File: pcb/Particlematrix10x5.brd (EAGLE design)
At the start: 100 x 80 mm, 65 parts

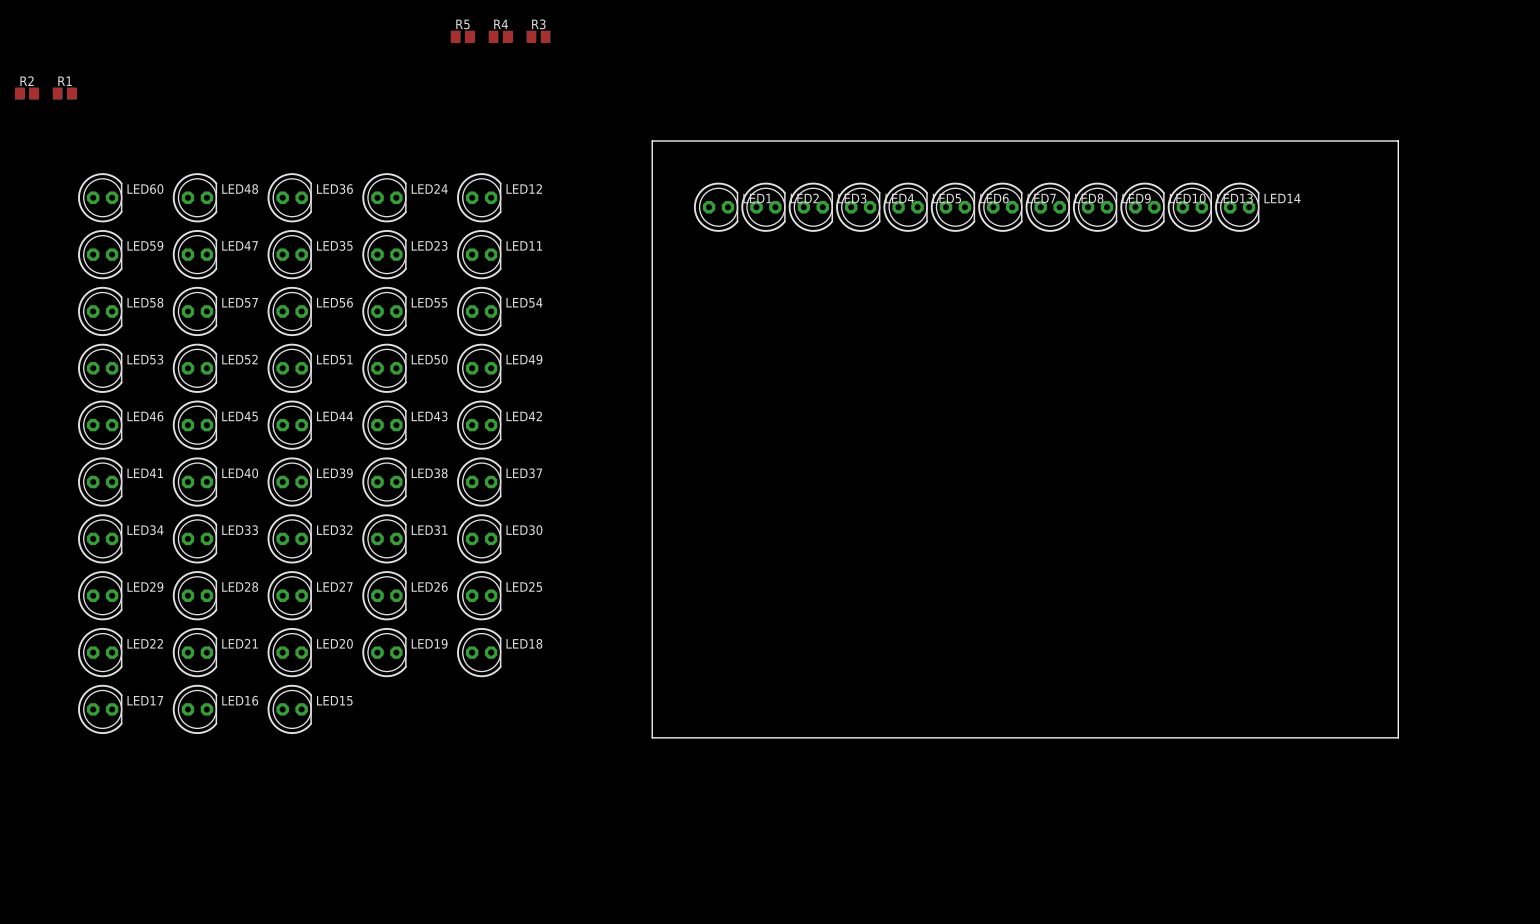
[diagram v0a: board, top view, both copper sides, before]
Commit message: Added 4017 decade counter to schematic
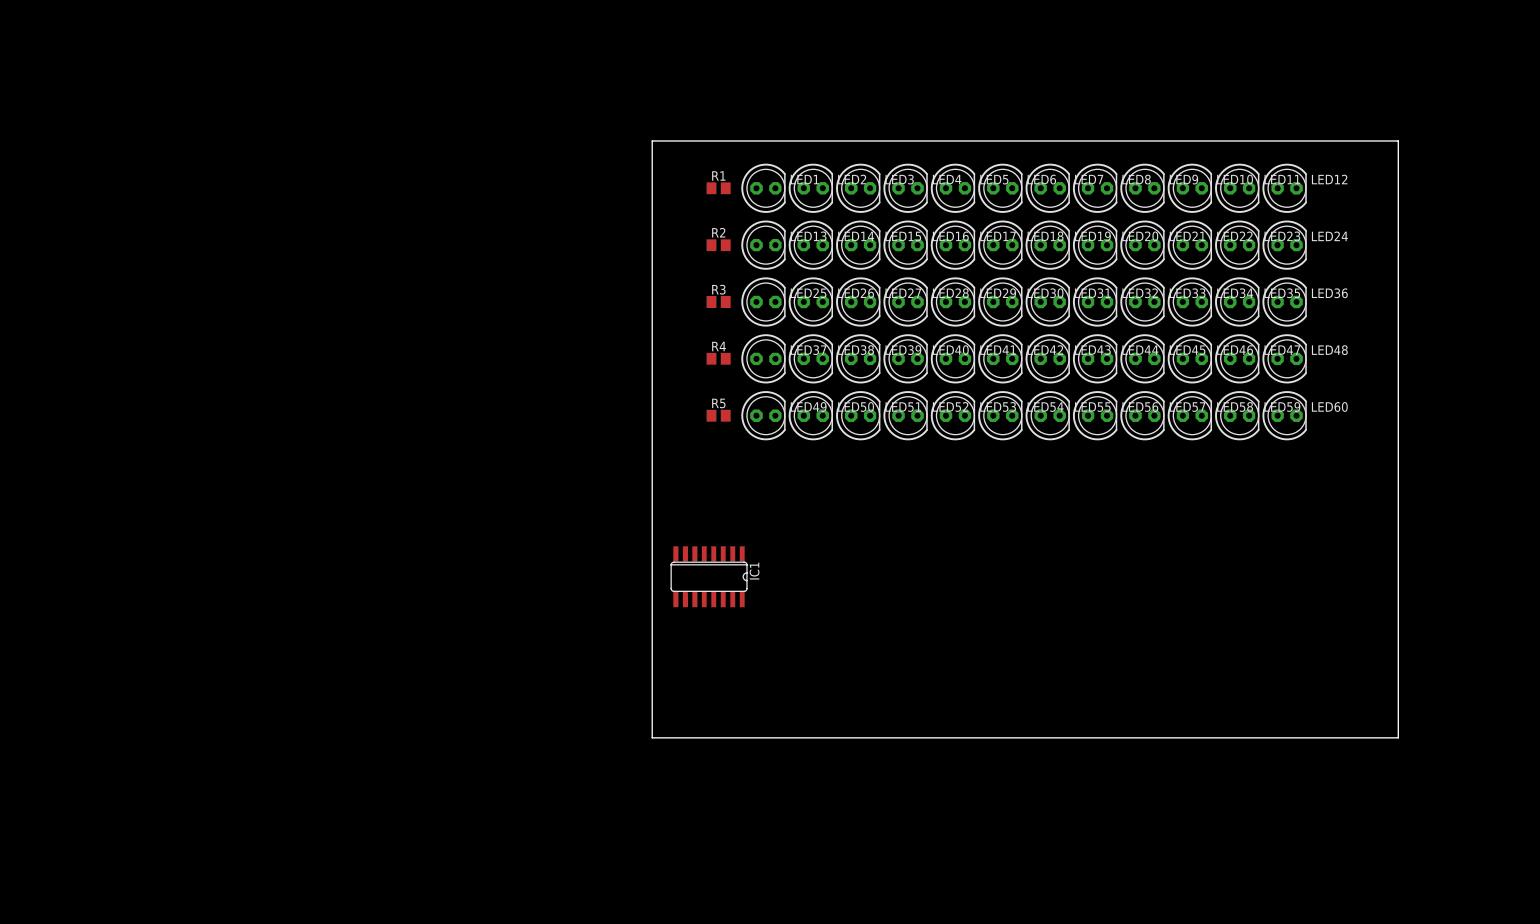
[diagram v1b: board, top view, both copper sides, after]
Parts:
- added IC1: 4017D, 40xx:SO16
- moved LED60 161.4 mm to (85.1, 43.2)
- moved LED22 155.9 mm to (72.4, 66.0)
- moved LED59 153.9 mm to (78.7, 43.2)
- moved LED34 149.5 mm to (72.4, 58.4)
- moved LED48 147.6 mm to (85.1, 50.8)
- moved LED58 146.7 mm to (72.4, 43.2)
- moved LED46 146.3 mm to (72.4, 50.8)
- moved LED47 140.4 mm to (78.7, 50.8)
- moved LED21 138.2 mm to (66.0, 66.0)
- moved LED36 134.1 mm to (85.1, 58.4)
- moved LED33 130.9 mm to (66.0, 58.4)
- moved LED17 130.1 mm to (40.6, 66.0)
- moved LED57 127.8 mm to (66.0, 43.2)
- moved LED45 127.3 mm to (66.0, 50.8)
- moved LED35 127.2 mm to (78.7, 58.4)
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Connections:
- removed net ROW1: R1.1
- removed net ROW2: R2.1
- removed net ROW3: R3.1
- removed net ROW4: R4.1
- removed net ROW5: R5.1
- new net N$1: IC1.3, R1.1
- new net N$2: IC1.2, R2.1
- new net N$3: IC1.4, R3.1
- new net N$4: IC1.7, R4.1
- new net N$5: IC1.10, R5.1
- new net N$6: IC1.1, IC1.15
- new net VDD: IC1.16
- new net VSS: IC1.8

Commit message: Routed all LEDs, decade counter, and Arduino Mega
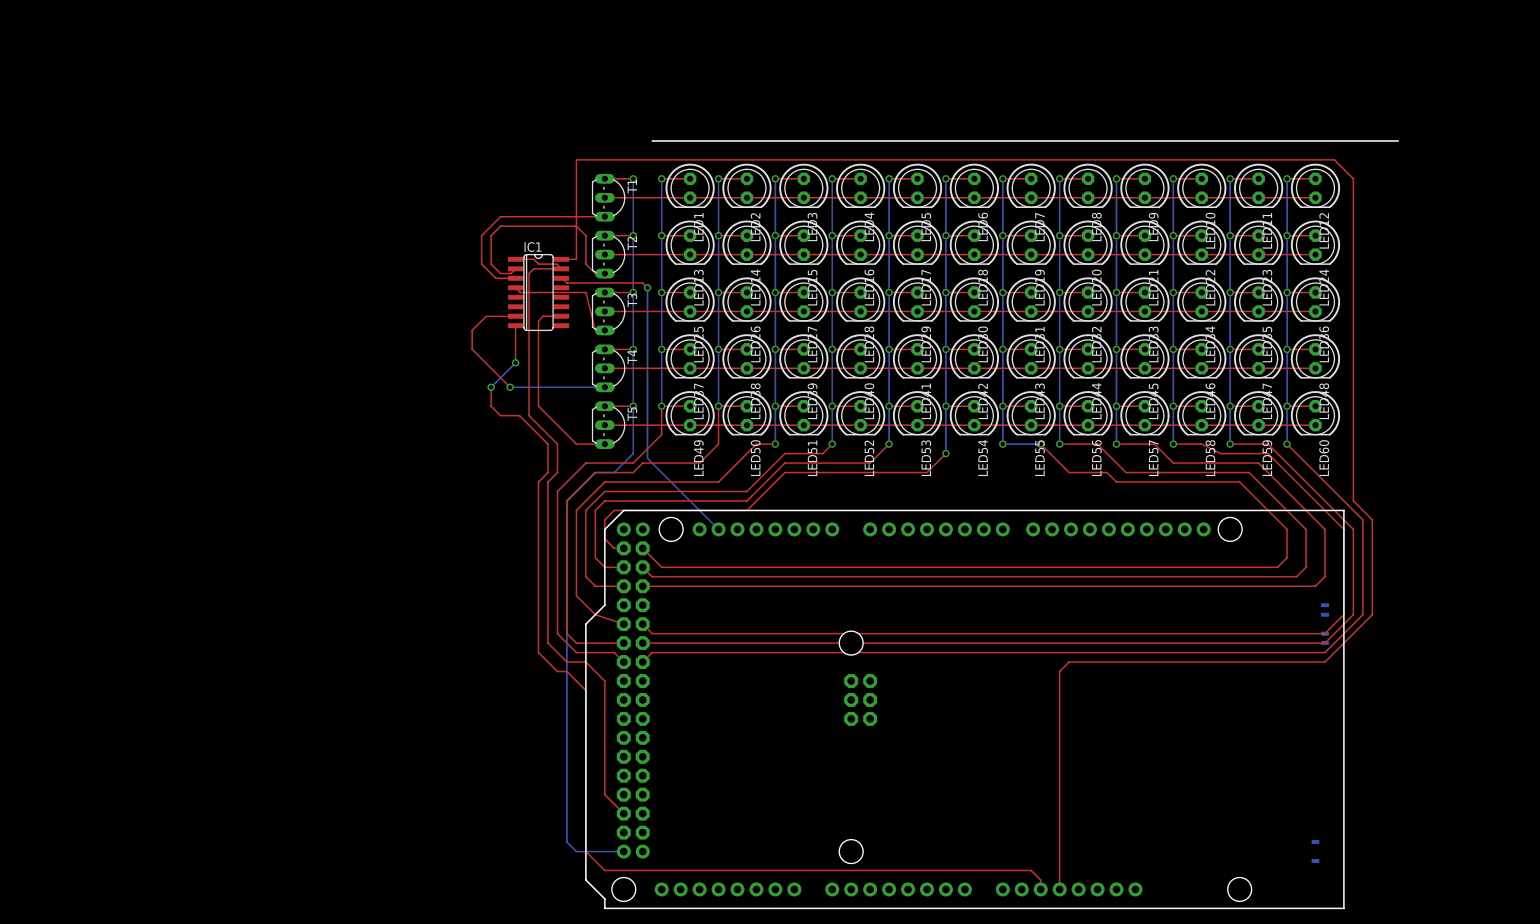
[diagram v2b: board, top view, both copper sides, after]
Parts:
- removed R1, R2, R3, R4, R5: 120, resistor:M0805
- added PCB1: ARDUINO_MEGA2560, E14_Arduino_revB:ARDUINO_MEGA2560
- added T1, T2, T3, T4, T5: (no value), transistor-neu-to92:TO92-EBC
- moved IC1 44.4 mm to (-15.2, 59.7), turned to 270 degrees
- moved LED1 10.2 mm to (5.08, 73.7), turned to 270 degrees
- moved LED13 10.2 mm to (5.08, 66.0), turned to 270 degrees
- moved LED25 10.2 mm to (5.08, 58.4), turned to 270 degrees
- moved LED37 10.2 mm to (5.08, 50.8), turned to 270 degrees
- moved LED49 10.2 mm to (5.08, 43.2), turned to 270 degrees
- moved LED14 8.89 mm to (12.7, 66.0), turned to 270 degrees
- moved LED2 8.89 mm to (12.7, 73.7), turned to 270 degrees
- moved LED26 8.89 mm to (12.7, 58.4), turned to 270 degrees
- moved LED38 8.89 mm to (12.7, 50.8), turned to 270 degrees
- moved LED50 8.89 mm to (12.7, 43.2), turned to 270 degrees
- moved LED15 7.62 mm to (20.3, 66.0), turned to 270 degrees
- moved LED27 7.62 mm to (20.3, 58.4), turned to 270 degrees
- moved LED3 7.62 mm to (20.3, 73.7), turned to 270 degrees
- moved LED39 7.62 mm to (20.3, 50.8), turned to 270 degrees
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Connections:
- removed net $1: LED1.K, LED10.K, LED11.K, LED12.K, LED2.K, LED3.K, LED4.K, LED5.K, LED6.K, LED7.K, LED8.K, LED9.K, R1.2
- removed net $2: LED13.K, LED14.K, LED15.K, LED16.K, LED17.K, LED18.K, LED19.K, LED20.K, LED21.K, LED22.K, LED23.K, LED24.K, R2.2
- removed net $3: LED25.K, LED26.K, LED27.K, LED28.K, LED29.K, LED30.K, LED31.K, LED32.K, LED33.K, LED34.K, LED35.K, LED36.K, R3.2
- removed net $4: LED37.K, LED38.K, LED39.K, LED40.K, LED41.K, LED42.K, LED43.K, LED44.K, LED45.K, LED46.K, LED47.K, LED48.K, R4.2
- removed net $9: LED49.K, LED50.K, LED51.K, LED52.K, LED53.K, LED54.K, LED55.K, LED56.K, LED57.K, LED58.K, LED59.K, LED60.K, R5.2
- removed net VDD: IC1.16
- removed net VSS: IC1.8
- new net GND: PCB1.GND..., PCB1.GND...., T1.E, T2.E, T3.E, T4.E, T5.E
- new net N$7: IC1.14, PCB1.20
- new net N$8: IC1.1, IC1.15, PCB1.51
- new net N$9: IC1.8, PCB1.GND..
- new net ROW1: LED1.K, LED10.K, LED11.K, LED12.K, LED2.K, LED3.K, LED4.K, LED5.K, LED6.K, LED7.K, LED8.K, LED9.K, T1.B
- new net ROW2: LED13.K, LED14.K, LED15.K, LED16.K, LED17.K, LED18.K, LED19.K, LED20.K, LED21.K, LED22.K, LED23.K, LED24.K, T2.B
- new net ROW3: LED25.K, LED26.K, LED27.K, LED28.K, LED29.K, LED30.K, LED31.K, LED32.K, LED33.K, LED34.K, LED35.K, LED36.K, T3.B
- new net ROW4: LED37.K, LED38.K, LED39.K, LED40.K, LED41.K, LED42.K, LED43.K, LED44.K, LED45.K, LED46.K, LED47.K, LED48.K, T4.B
- new net ROW5: LED49.K, LED50.K, LED51.K, LED52.K, LED53.K, LED54.K, LED55.K, LED56.K, LED57.K, LED58.K, LED59.K, LED60.K, T5.B
- net COL1: now also PCB1.35
- net COL10: now also PCB1.30
- net COL11: now also PCB1.32
- net COL12: now also PCB1.34
- net COL2: now also PCB1.33
- net COL3: now also PCB1.31
- net COL4: now also PCB1.27
- net COL5: now also PCB1.25
- net COL6: now also PCB1.23
- net COL7: now also PCB1.22
- net COL8: now also PCB1.24
- net COL9: now also PCB1.26
- net N$1: now also T1.C; no longer R1.1
- net N$2: now also T2.C; no longer R2.1
- net N$3: now also T3.C; no longer R3.1
- net N$4: now also T4.C; no longer R4.1
- net N$5: now also T5.C; no longer R5.1
- net N$6: now also IC1.16, PCB1.5V; no longer IC1.1, IC1.15
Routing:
- net N$6: track 0.00 -> 254.3 mm
- net COL7: track 0.00 -> 189.2 mm, vias 0 -> 7
- net COL10: track 0.00 -> 189.0 mm, vias 0 -> 6
- net COL8: track 0.00 -> 187.4 mm, vias 0 -> 6
- net COL9: track 0.00 -> 185.6 mm, vias 0 -> 6
- net COL11: track 0.00 -> 184.1 mm, vias 0 -> 6
- net COL12: track 0.00 -> 180.8 mm, vias 0 -> 6
- net N$9: track 0.00 -> 144.2 mm, vias 0 -> 2
- net GND: track 0.00 -> 121.3 mm, vias 0 -> 5
- net COL6: track 0.00 -> 110.9 mm, vias 0 -> 6
- net COL5: track 0.00 -> 108.3 mm, vias 0 -> 6
- net COL2: track 0.00 -> 107.8 mm, vias 0 -> 5
- net COL4: track 0.00 -> 105.8 mm, vias 0 -> 6
- net COL3: track 0.00 -> 104.0 mm, vias 0 -> 6
- net COL1: track 0.00 -> 100.0 mm, vias 0 -> 5
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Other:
- board size 100 x 80 mm -> 101.6 x 53.3 mm

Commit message: Fix routing errors on pcb
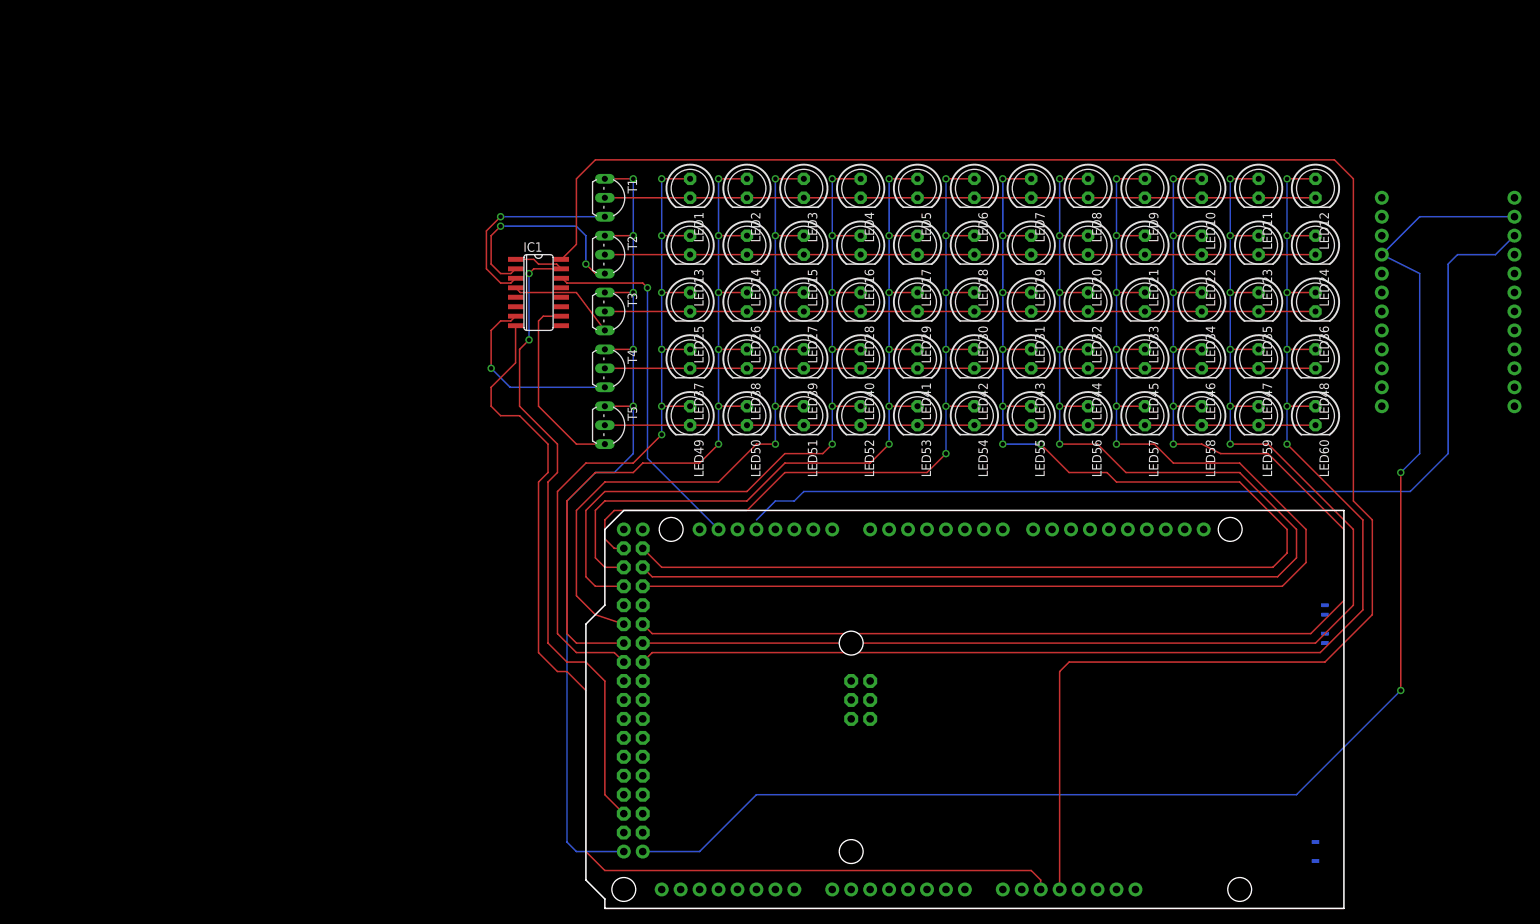
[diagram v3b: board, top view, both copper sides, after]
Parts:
- added U$1: SPARK_CORECORE, Spark:SPARK_CORE
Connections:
- new net N$10: PCB1.18, U$1.3
- new net RAW: U$1.1
- new net VCC: U$1.24
- new net VDDA: U$1.22
- net GND: now also U$1.2, U$1.21
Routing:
- net GND: track 121.3 -> 314.3 mm, vias 5 -> 7
- net N$10: track 0.00 -> 132.3 mm
- net COL9: track 185.6 -> 179.4 mm
- net N$4: track 29.1 -> 25.4 mm
- net COL8: track 187.4 -> 184.1 mm
- net N$6: track 254.3 -> 251.6 mm
- net N$3: track 16.2 -> 14.8 mm
- net COL10: track 189.0 -> 187.9 mm
- net N$8: track 91.5 -> 92.5 mm, vias 0 -> 2
- net COL11: track 184.1 -> 183.4 mm
- net N$1: vias 0 -> 1
- net N$9: vias 2 -> 0
- net N$2: vias 0 -> 2
- net COL2: vias 5 -> 6
- net COL1: vias 5 -> 6

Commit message: Mirrored Arduino and Spark Core again to face front; rerouted
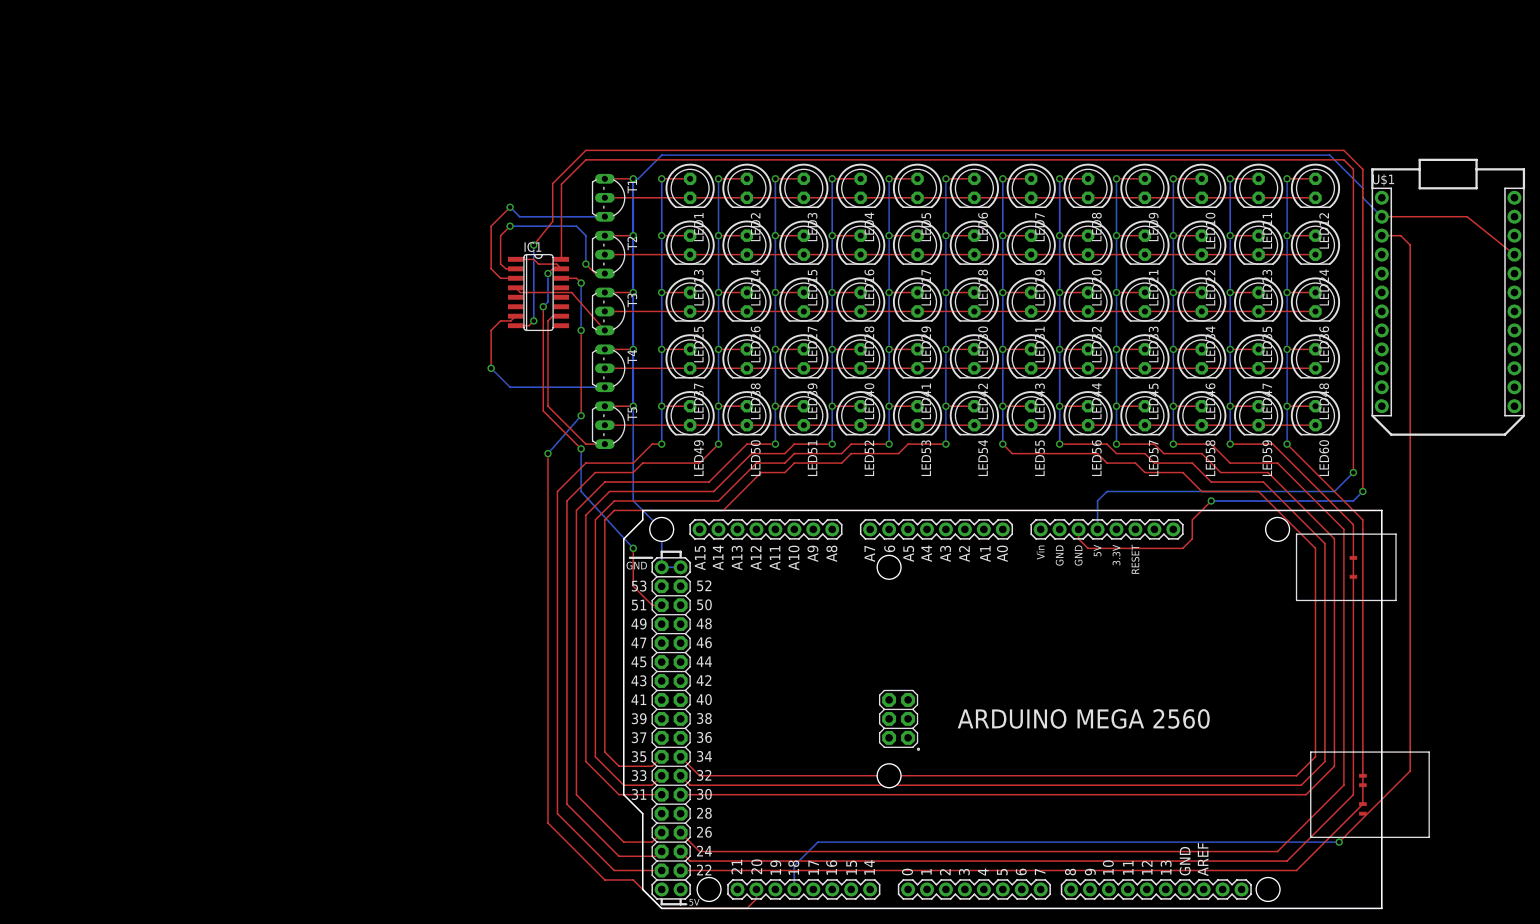
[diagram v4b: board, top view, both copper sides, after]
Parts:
- moved PCB1 53.6 mm to (97.8, 30.5), flipped to the top, turned to 180 degrees
- flipped U$1 to the top
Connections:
- net COL1: now also PCB1.23; no longer PCB1.35
- net COL10: now also PCB1.26; no longer PCB1.30
- net COL11: now also PCB1.24; no longer PCB1.32
- net COL12: now also PCB1.22; no longer PCB1.34
- net COL2: now also PCB1.25; no longer PCB1.33
- net COL3: now also PCB1.27; no longer PCB1.31
- net COL4: now also PCB1.31; no longer PCB1.27
- net COL5: now also PCB1.33; no longer PCB1.25
- net COL6: now also PCB1.35; no longer PCB1.23
- net COL7: now also PCB1.34; no longer PCB1.22
- net COL8: now also PCB1.32; no longer PCB1.24
- net COL9: now also PCB1.30; no longer PCB1.26
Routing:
- net N$9: track 144.2 -> 221.2 mm, vias 0 -> 4
- net N$7: track 48.3 -> 111.4 mm, vias 1 -> 4
- net GND: track 314.3 -> 253.9 mm, vias 7 -> 5
- net N$6: track 251.6 -> 198.4 mm, vias 0 -> 1
- net COL6: track 110.9 -> 144.6 mm
- net COL3: track 104.0 -> 137.6 mm
- net N$10: track 132.3 -> 165.8 mm, vias 0 -> 1
- net COL5: track 108.3 -> 140.9 mm
- net N$8: track 92.5 -> 60.6 mm, vias 2 -> 4
- net COL1: track 100.0 -> 131.5 mm
- net COL4: track 105.8 -> 136.6 mm
- net COL2: track 107.8 -> 138.4 mm
- net COL9: track 179.4 -> 208.8 mm
- net COL8: track 184.1 -> 213.1 mm
- net COL7: track 188.8 -> 217.4 mm, vias 7 -> 6
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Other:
- outline, holes or cut-outs redrawn
